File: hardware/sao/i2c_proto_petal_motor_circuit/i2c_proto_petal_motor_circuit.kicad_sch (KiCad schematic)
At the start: 10 parts, among them M1 Motor_DC, Q1 2N2222 (NPN), SW1 SW_Push, U1 CH32V003FxPx, U2 CH32V003f4p6

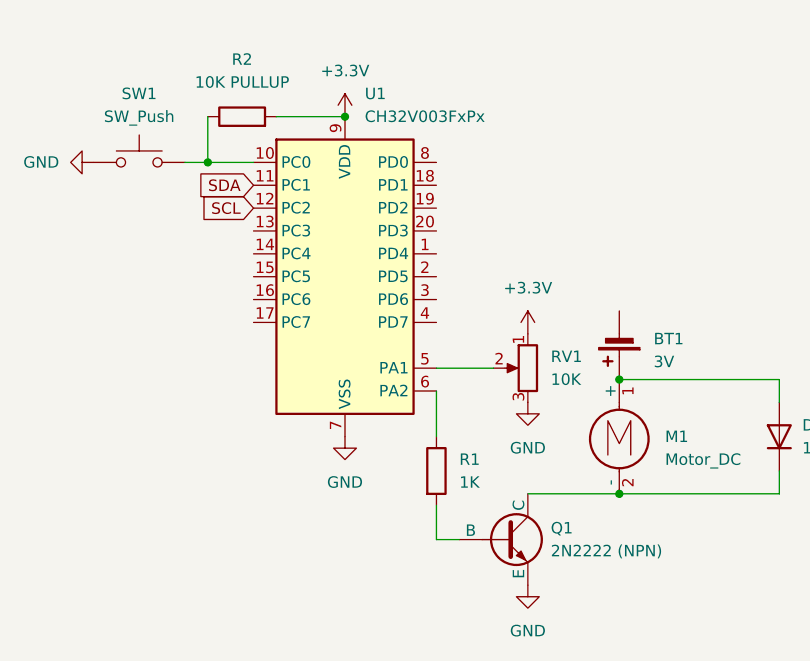
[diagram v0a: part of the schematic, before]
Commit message: added some code examples as a starting point for the motor circuit
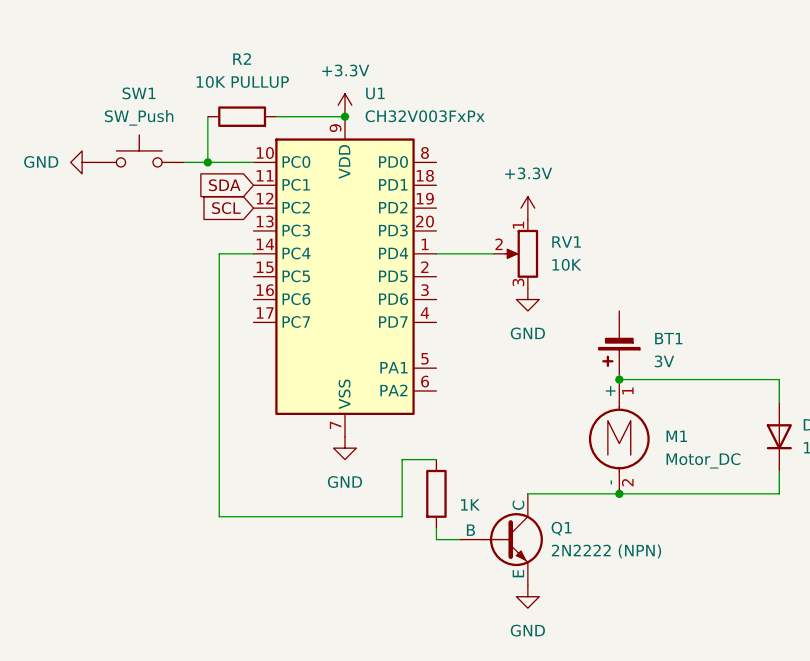
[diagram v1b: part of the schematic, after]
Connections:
- net at RV1.2: now also U1.1 (PD4); no longer U1.5 (PA1)
- net at R1.1: now also U1.14 (PC4); no longer U1.6 (PA2)
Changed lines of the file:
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@@
 	(wire
 		(pts
-			(xy 157.48 93.98) (xy 157.48 99.06)
-		)
-		(stroke
-			(width 0)
-			(type default)
-		)
-	)
-	(wire
-		(pts
-			(xy 157.48 106.68) (xy 157.48 110.49)
+			(xy 153.67 101.6) (xy 157.48 101.6)
+		)
+		(stroke
+			(width 0)
+			(type default)
+		)
+	)
+	(wire
+		(pts
+			(xy 133.35 78.74) (xy 133.35 107.95)
+		)
+		(stroke
+			(width 0)
+			(type default)
+		)
+	)
+	(wire
+		(pts
+			(xy 157.48 109.22) (xy 157.48 110.49)
 		)
 		(stroke
@@
 	(wire
 		(pts
-			(xy 157.48 91.44) (xy 163.83 91.44)
+			(xy 157.48 78.74) (xy 163.83 78.74)
+		)
+		(stroke
+			(width 0)
+			(type default)
+		)
+	)
+	(wire
+		(pts
+			(xy 137.16 78.74) (xy 133.35 78.74)
 		)
 		(stroke
@@
 	(wire
 		(pts
+			(xy 153.67 107.95) (xy 153.67 101.6)
+		)
+		(stroke
+			(width 0)
+			(type default)
+		)
+	)
+	(wire
+		(pts
 			(xy 195.58 105.41) (xy 177.8 105.41)
 		)
@@
 		(pts
 			(xy 129.54 68.58) (xy 132.08 68.58)
+		)
+		(stroke
+			(width 0)
+			(type default)
+		)
+	)
+	(wire
+		(pts
+			(xy 133.35 107.95) (xy 153.67 107.95)
 		)
 		(stroke
@@
 	(symbol
 		(lib_id "power:GND")
-		(at 167.64 95.25 0)
-		(unit 1)
-		(exclude_from_sim no)
-		(in_bom yes)
-		(on_board yes)
-		(dnp no)
-		(fields_autoplaced yes)
-		(property "Reference" "#PWR01"
-			(at 167.64 101.6 0)
+		(at 167.64 82.55 0)
+		(unit 1)
+		(exclude_from_sim no)
+		(in_bom yes)
+		(on_board yes)
+		(dnp no)
+		(fields_autoplaced yes)
+		(property "Reference" "#PWR02"
+			(at 167.64 88.9 0)
 			(effects
 				(font
@@
 		)
 		(property "Value" "GND"
-			(at 167.64 100.33 0)
+			(at 167.64 87.63 0)
 			(effects
 				(font
@@
 		)
 		(property "Footprint" ""
-			(at 167.64 95.25 0)
+			(at 167.64 82.55 0)
 			(effects
 				(font
@@
 		)
 		(property "Datasheet" ""
-			(at 167.64 95.25 0)
+			(at 167.64 82.55 0)
 			(effects
 				(font
@@
 		)
 		(property "Description" "Power symbol creates a global label with name \"GND\" , ground"
-			(at 167.64 95.25 0)
-			(effects
-				(font
-					(size 1.27 1.27)
-				)
-				(hide yes)
-			)
-		)
-		(pin "1"
-		)
-		(instances
-			(project ""
-				(path "/3de0a0a4-d182-4a02-a503-5dc1a3cc2679"
-					(reference "#PWR01")
+			(at 167.64 82.55 0)
+			(effects
+				(font
+					(size 1.27 1.27)
+				)
+				(hide yes)
+			)
+		)
+		(pin "1"
+		)
+		(instances
+			(project "i2c_proto_petal_motor_circuit"
+				(path "/3de0a0a4-d182-4a02-a503-5dc1a3cc2679"
+					(reference "#PWR02")
 					(unit 1)
 				)
@@
 	)
 	(symbol
-		(lib_id "power:+3.3V")
-		(at 167.64 87.63 0)
-		(unit 1)
-		(exclude_from_sim no)
-		(in_bom yes)
-		(on_board yes)
-		(dnp no)
-		(fields_autoplaced yes)
-		(property "Reference" "#PWR02"
-			(at 167.64 91.44 0)
-			(effects
-				(font
-					(size 1.27 1.27)
-				)
-				(hide yes)
-			)
-		)
-		(property "Value" "+3.3V"
-			(at 167.64 82.55 0)
-			(effects
-				(font
-					(size 1.27 1.27)
-				)
-			)
-		)
-		(property "Footprint" ""
-			(at 167.64 87.63 0)
-			(effects
-				(font
-					(size 1.27 1.27)
-				)
-				(hide yes)
-			)
-		)
-		(property "Datasheet" ""
-			(at 167.64 87.63 0)
-			(effects
-				(font
-					(size 1.27 1.27)
-				)
-				(hide yes)
-			)
-		)
-		(property "Description" "Power symbol creates a global label with name \"+3.3V\""
-			(at 167.64 87.63 0)
-			(effects
-				(font
-					(size 1.27 1.27)
-				)
-				(hide yes)
-			)
-		)
-		(pin "1"
-		)
-		(instances
-			(project ""
-				(path "/3de0a0a4-d182-4a02-a503-5dc1a3cc2679"
-					(reference "#PWR02")
-					(unit 1)
-				)
-			)
-		)
-	)
-	(symbol
 		(lib_id "Diode:1N4001")
 		(at 195.58 99.06 90)
@@
 	(symbol
 		(lib_id "Device:R_Potentiometer")
-		(at 167.64 91.44 0)
+		(at 167.64 78.74 0)
 		(mirror y)
 		(unit 1)
@@
 		(dnp no)
 		(property "Reference" "RV1"
-			(at 170.18 90.1699 0)
+			(at 170.18 77.4699 0)
 			(effects
 				(font
@@
 		)
 		(property "Value" "10K"
-			(at 170.18 92.7099 0)
+			(at 170.18 80.0099 0)
 			(effects
 				(font
@@
 		)
 		(property "Footprint" ""
-			(at 167.64 91.44 0)
+			(at 167.64 78.74 0)
 			(effects
 				(font
@@
 		)
 		(property "Datasheet" "~"
-			(at 167.64 91.44 0)
+			(at 167.64 78.74 0)
 			(effects
 				(font
@@
 		)
 		(property "Description" "Potentiometer"
-			(at 167.64 91.44 0)
+			(at 167.64 78.74 0)
 			(effects
 				(font
@@
 		)
 		(instances
-			(project ""
+			(project "i2c_proto_petal_motor_circuit"
 				(path "/3de0a0a4-d182-4a02-a503-5dc1a3cc2679"
 					(reference "RV1")
@@
 	(symbol
 		(lib_id "Device:R")
-		(at 157.48 102.87 0)
+		(at 157.48 105.41 0)
 		(unit 1)
 		(exclude_from_sim no)
@@
 		(fields_autoplaced yes)
 		(property "Reference" "R1"
-			(at 160.02 101.5999 0)
+			(at 160.02 104.1399 0)
 			(effects
 				(font
@@
 				)
 				(justify left)
+				(hide yes)
 			)
 		)
 		(property "Value" "1K"
-			(at 160.02 104.1399 0)
+			(at 160.02 106.6799 0)
 			(effects
 				(font
@@
 		)
 		(property "Footprint" ""
-			(at 155.702 102.87 90)
+			(at 155.702 105.41 90)
 			(effects
 				(font
@@
 		)
 		(property "Datasheet" "~"
-			(at 157.48 102.87 0)
+			(at 157.48 105.41 0)
 			(effects
 				(font
@@
 		)
 		(property "Description" "Resistor"
-			(at 157.48 102.87 0)
+			(at 157.48 105.41 0)
 			(effects
 				(font
@@
 					(unit 1)
 				)
+			)
+		)
+	)
+	(symbol
+		(lib_id "power:+3.3V")
+		(at 167.64 74.93 0)
+		(unit 1)
+		(exclude_from_sim no)
+		(in_bom yes)
+		(on_board yes)
+		(dnp no)
+		(fields_autoplaced yes)
+		(property "Reference" "#PWR01"
+			(at 167.64 78.74 0)
+			(effects
+				(font
+					(size 1.27 1.27)
+				)
+				(hide yes)
+			)
+		)
+		(property "Value" "+3.3V"
+			(at 167.64 69.85 0)
+			(effects
+				(font
+					(size 1.27 1.27)
+				)
+			)
+		)
+		(property "Footprint" ""
+			(at 167.64 74.93 0)
+			(effects
+				(font
+					(size 1.27 1.27)
+				)
+				(hide yes)
+			)
+		)
+		(property "Datasheet" ""
+			(at 167.64 74.93 0)
+			(effects
+				(font
+					(size 1.27 1.27)
+				)
+				(hide yes)
+			)
+		)
+		(property "Description" "Power symbol creates a global label with name \"+3.3V\""
+			(at 167.64 74.93 0)
+			(effects
+				(font
+					(size 1.27 1.27)
+				)
+				(hide yes)
+			)
+		)
+		(pin "1"
+		)
+		(instances
+			(project "i2c_proto_petal_motor_circuit"
+				(path "/3de0a0a4-d182-4a02-a503-5dc1a3cc2679"
+					(reference "#PWR01")
+					(unit 1)
+				)

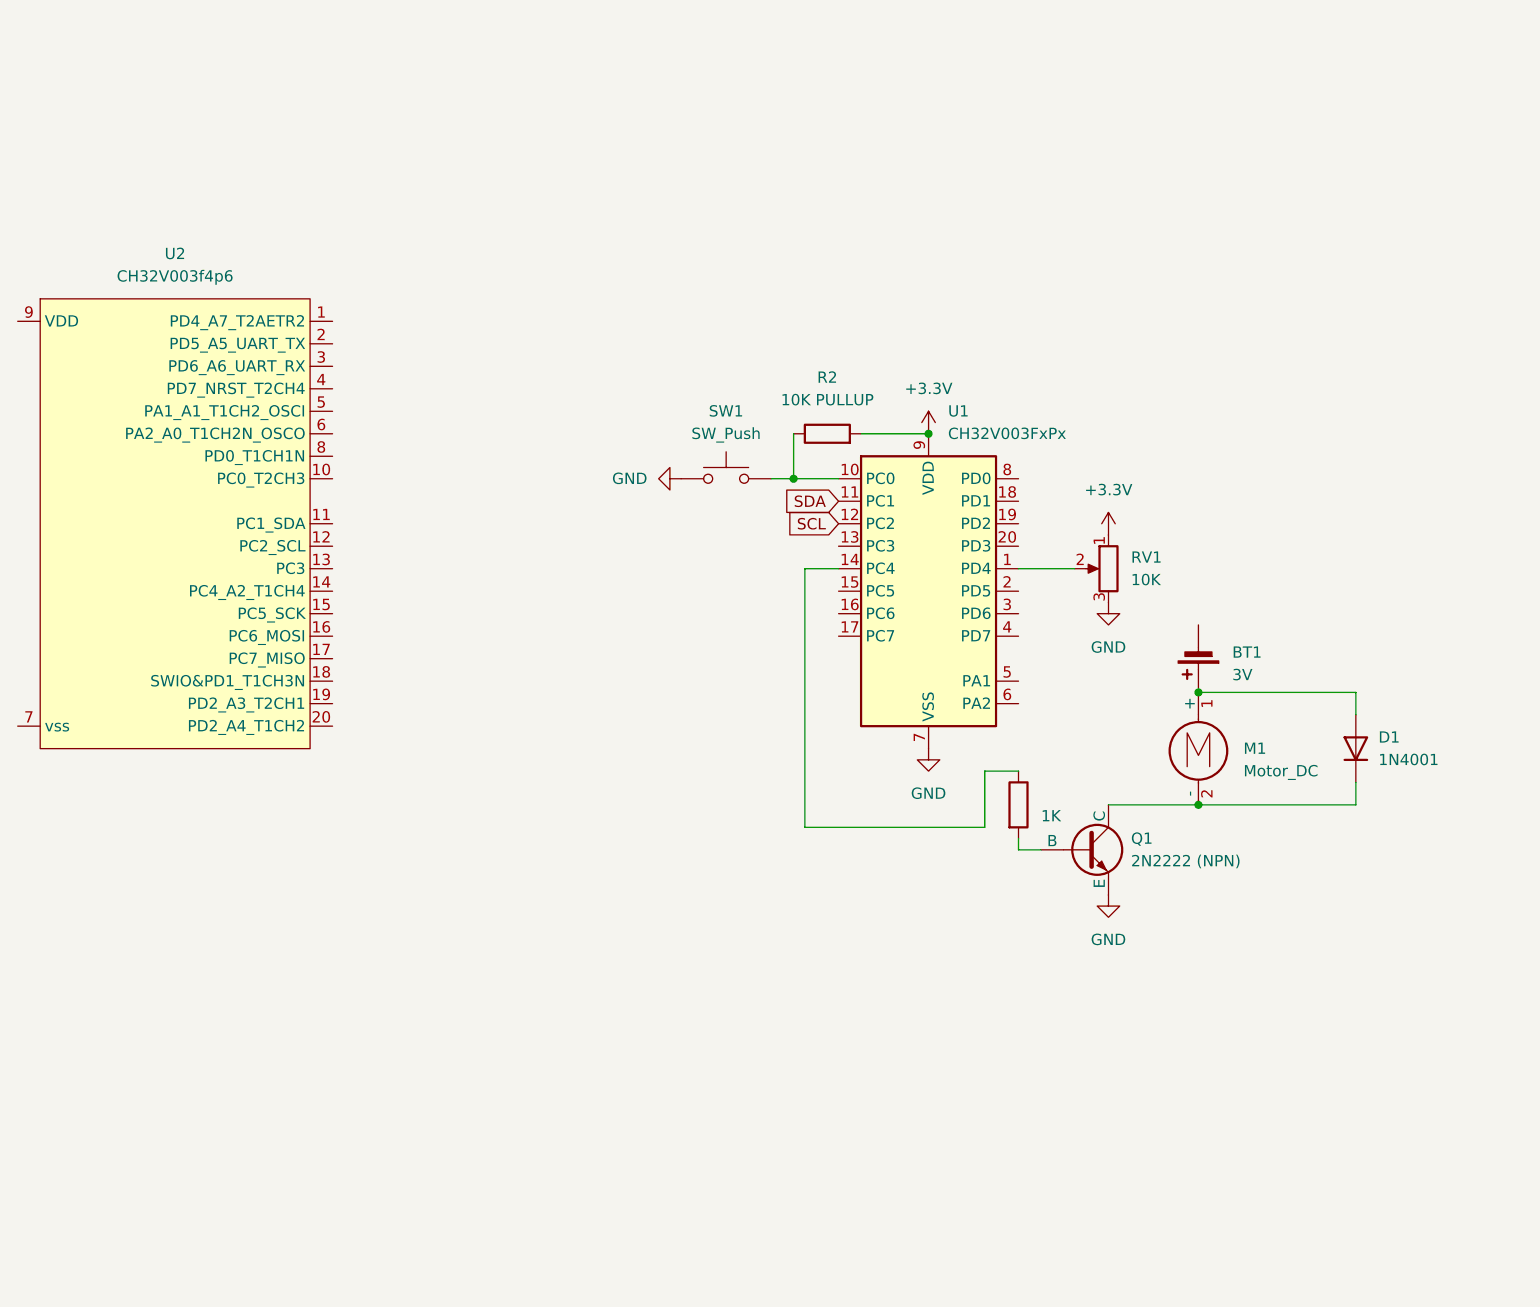
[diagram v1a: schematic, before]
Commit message: updated schematic to represent all three motor possibilities
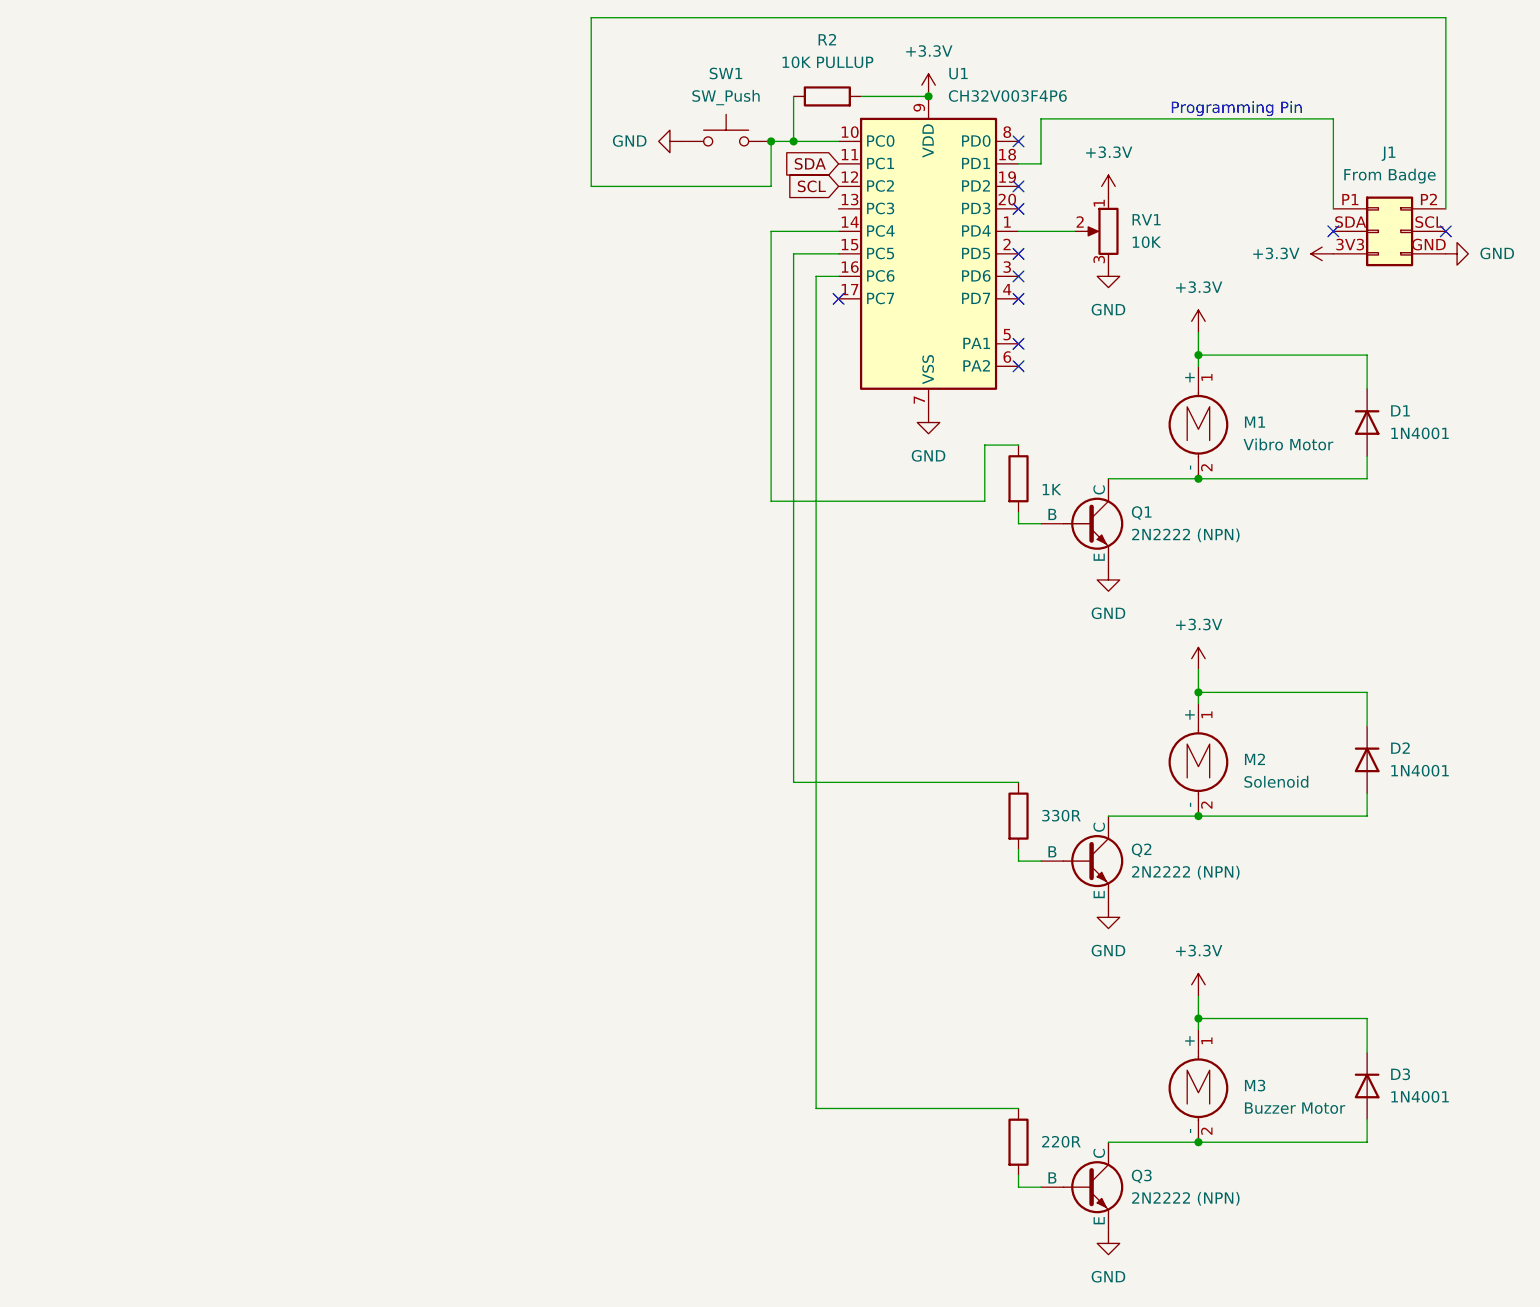
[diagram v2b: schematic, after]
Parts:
- removed BT1: 3V, symbol Device:Battery_Cell
- removed U2: CH32V003f4p6, Package_SO:TSSOP-20_4.4x6.5mm_P0.65mm, symbol CH32V003:CH32V003f4p6
- added D2, D3: 1N4001, Diode_THT:D_DO-41_SOD81_P10.16mm_Horizontal, symbol Diode:1N4001
- added J1: From Badge, 4ms_Connector:Pins_2x03_1.27mm_SMD, symbol PCM_4ms_Connector:Pins_02x03_P1.27mm_SMT
- added M2: Solenoid, symbol Motor:Motor_DC
- added M3: Buzzer Motor, symbol Motor:Motor_DC
- added Q2, Q3: 2N2222 (NPN), symbol Simulation_SPICE:NPN
- added R3: 330R, symbol Device:R
- added R4: 220R, symbol Device:R
- M1: value Motor_DC -> Vibro Motor
- U1: value CH32V003FxPx -> CH32V003F4P6
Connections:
- net +3.3V: now also D1.1 (K), M1.1 (+), D2.1 (K), D3.1 (K), J1.3V3 (GND), M2.1 (+), M3.1 (+)
- net GND: now also J1.GND, Q2.3 (E), Q3.3 (E)
- net at M1.2 (-), Q1.1 (C): now also D1.2 (A); no longer D1.1 (K)
- net at R2.1, SW1.2, U1.10 (PC0): now also J1.P2 (+12V)
- net at U1.15 (PC5): now also R3.1
- net at U1.16 (PC6): now also R4.1
- net at U1.18 (PD1): now also J1.P1 (+12V)
- new net: D3.2 (A), M3.2 (-), Q3.1 (C)
- new net: Q3.2 (B), R4.2
- new net: D2.2 (A), M2.2 (-), Q2.1 (C)
- new net: Q2.2 (B), R3.2
- no-connect marks 0 -> 11
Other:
- note added: "Programming Pin"
- moved on the sheet: D1, M1, Q1, R2, RV1, SW1, U1
